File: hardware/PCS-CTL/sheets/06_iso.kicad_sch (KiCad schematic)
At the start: 28 parts, among them J601 KF2EDGR-3.81-6P, J602 KF2EDGR-3.81-6P, U601 CA-IS3050W, U602 CA-IS3082WNX, U603 CA-IS3821LG, U604 CA-IS3821LG, U605 CA-IS3820LG

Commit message: Complete the inverter control board PCS-CTL rev A0 for the three-wire build (D-064)
Grid-voltage, residual-current and temperature signals into the ADC, the second AC contactor through the
trip latch, the residual-current test output and the inverter pin plan. 8 sheets, 305 parts, 209 nets; every
build check passes; the PV control board's outputs are unchanged. The controller has 23 analog pins, not 25:
the eight temperature inputs share one pin through a multiplexer that is in no trip path. Module PCS-P125:
1,521 USD at catalogue prices, 1,292 USD at 5,000 units. Everything is calculated or estimated.

Co-Authored-By: Claude Fable 5.1 <noreply@anthropic.com>
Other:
- title: PV-CTL control board - Barrier B1: isolators, CAN, RS-485 -> PCS-CTL control board - Barrier B1: isolators, CAN, RS-485
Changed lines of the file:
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@@
 	(paper "A3")
 	(title_block
-		(title "PV-CTL control board - Barrier B1: isolators, CAN, RS-485")
+		(title "PCS-CTL control board - Barrier B1: isolators, CAN, RS-485")
 		(date "2026-10-05")
 		(rev "A0")

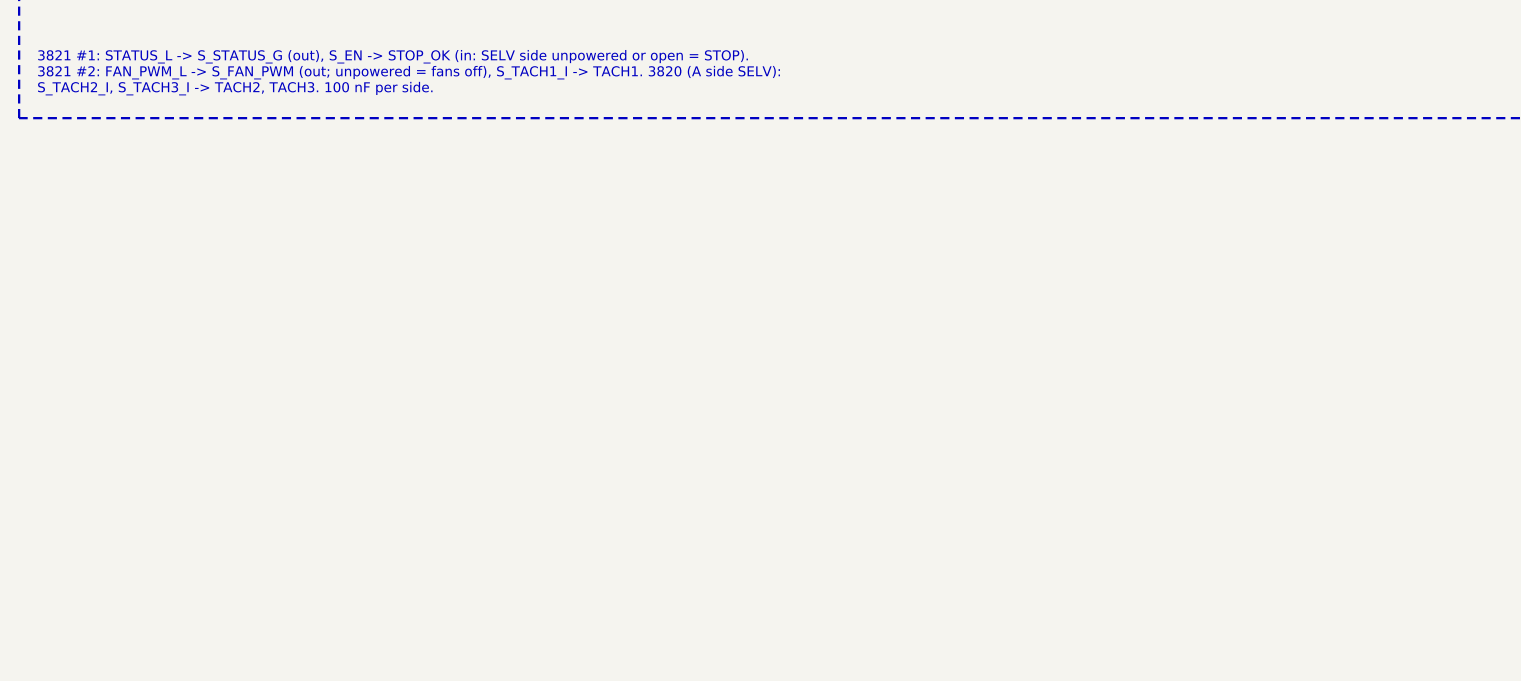
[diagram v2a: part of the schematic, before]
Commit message: Megarevo module parity: four-wire inverter, AC-side start-up, Ethernet and recorder on the control board, aux rev A3 (D-073..D-077)
- D-073 parity policy and register (modules only; PMA0125 and PMD-75-G3 sheets, PMA manual notes, catalogue 2026 manifest row)
- D-074 PCS-PWR-4W + PCS-CTL-4W = PCS-P125-4W drawn (fourth leg, L_N, 4-pole AC port, VGN, IL4), AC start-up tap and
  AC precharge on both builds, 30 firmware rows, declarations (kVA tiers, AC short-circuit coordination, airflow, precision)
- D-075 control board: CH9121T Ethernet bridge over CA-IS3842HW (fitted on PCS-CTL), GD25Q32E recorder flash replacing the
  EEPROM, chainable stop / ready / battery-fault inputs and HFD27 ready relay, port roles, altitude 2,000 m with the 15 mm
  isolator option specified, SELV logic allocation 2.2 W
- D-076 AUX-75 rev A3: live 30 W / 48 W for 1 s, one design for every module (turns 50:9:10, sense 3 x 0.866 ohm), four-wire
  DC precharge drawn at 200 ohm; D-077 control study: off-grid secondary restoration, THDu, imbalance, ride-through limiter
  with the stiff-grid derating rule, neutral-leg loop
- sim/compare_megarevo_pcs.py: PCS-P125 / PCS-P125-4W against the PMA0125 (2 better, 38 meets, 4 below, 9 not assessed, 0
  pending of 53); PV comparison 2 / 24 / 3 / 5 / 0 of 34 (standby 12.7 / 22.4 W)
- pin ledger E: control-board parts, shield-pin rule, fuse and connector notes (247 parts, 191 pass, 0 fail); review register
  PCM-14 and PCM-22 closed; magnetics re-run; all 15 boards rebuilt, BOMs, costs, audits and figures regenerated; README,
  guide 01-13 and the decisions mirror updated

Co-Authored-By: Claude Fable 5.1 <noreply@anthropic.com>
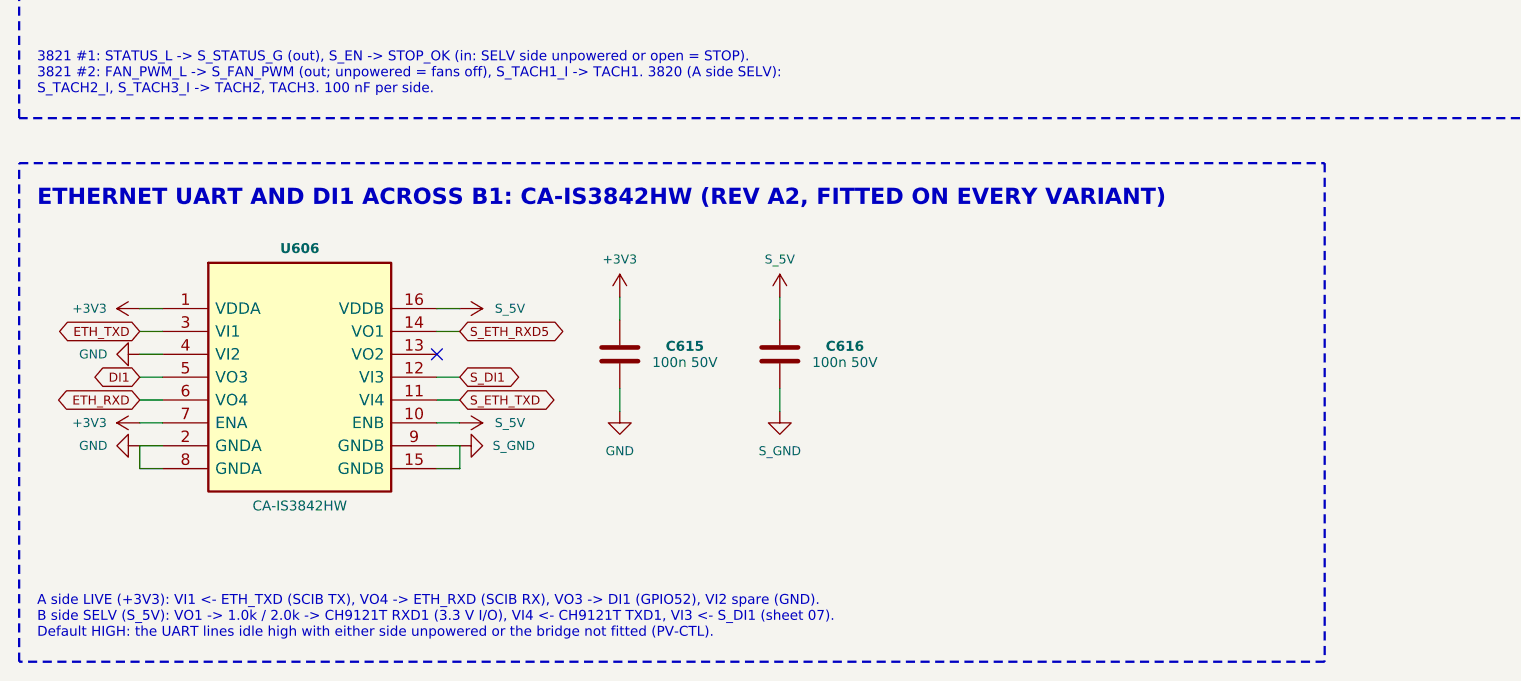
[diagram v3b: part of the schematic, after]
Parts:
- added C615, C616: 100n 50V, symbol dcdc:C
- added U606: CA-IS3842HW, symbol dcdc:CA_IS3842
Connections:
- net +3V3: now also C615.1, U606.1 (VDDA), U606.7 (ENA)
- net GND: now also C615.2, U606.2 (GNDA), U606.4 (VI2), U606.8 (GNDA)
- net S_5V: now also C616.1, U606.10 (ENB), U606.16 (VDDB)
- net S_GND: now also C616.2, U606.15 (GNDB), U606.9 (GNDB)
- new net DI1: U606.5 (VO3)
- new net ETH_RXD: U606.6 (VO4)
- new net ETH_TXD: U606.3 (VI1)
- new net S_DI1: U606.12 (VI3)
- new net S_ETH_RXD5: U606.14 (VO1)
- new net S_ETH_TXD: U606.11 (VI4)
- no-connect marks 7 -> 8
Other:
- note added: "A side LIVE (+3V3): VI1 <- ETH_TXD (SCIB TX), VO4 -> ETH_RXD (SCIB RX), VO3 -> DI1 (GPIO52), VI2 spare (GND). B side SELV (S_5V): VO1 -> 1.0k / 2.0k -> CH9121T RXD1 (3.3 V I/O), VI4 <- CH9121T TXD1, VI3 <- S_DI1 (sheet 07). Default HIGH: the UART lines idle high with either side unpowered or the bridge not fitted (PV-CTL)."
- note added: "ETHERNET UART AND DI1 ACROSS B1: CA-IS3842HW (REV A2, FITTED ON EVERY VARIANT)"
